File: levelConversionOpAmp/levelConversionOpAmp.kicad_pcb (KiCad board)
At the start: 2 copper layers, 38.1 x 61 mm, 23 parts, among them J1 IN, J2 OUT, J3 POW, Q1 PN2222A, Q2 PN2222A, U1 TL082

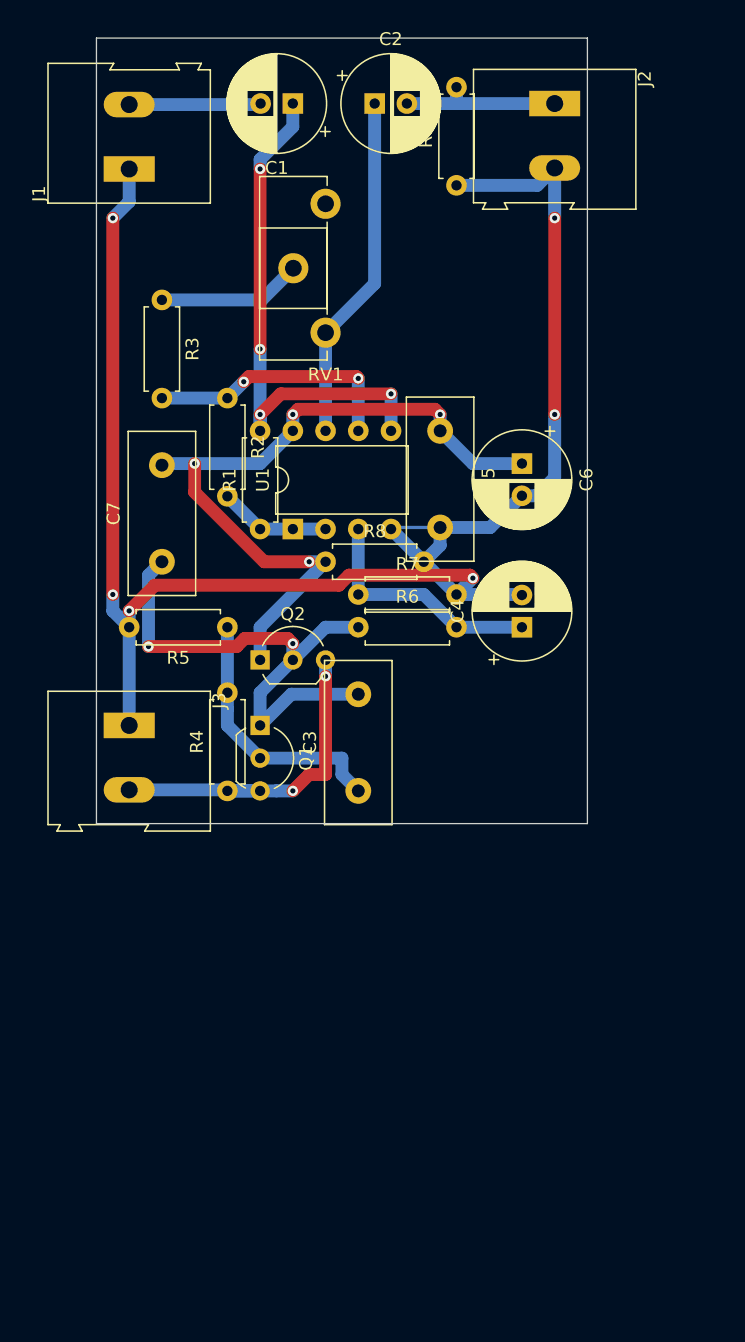
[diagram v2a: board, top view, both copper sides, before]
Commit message: Made PCB with surface mount and correct cap tolerances
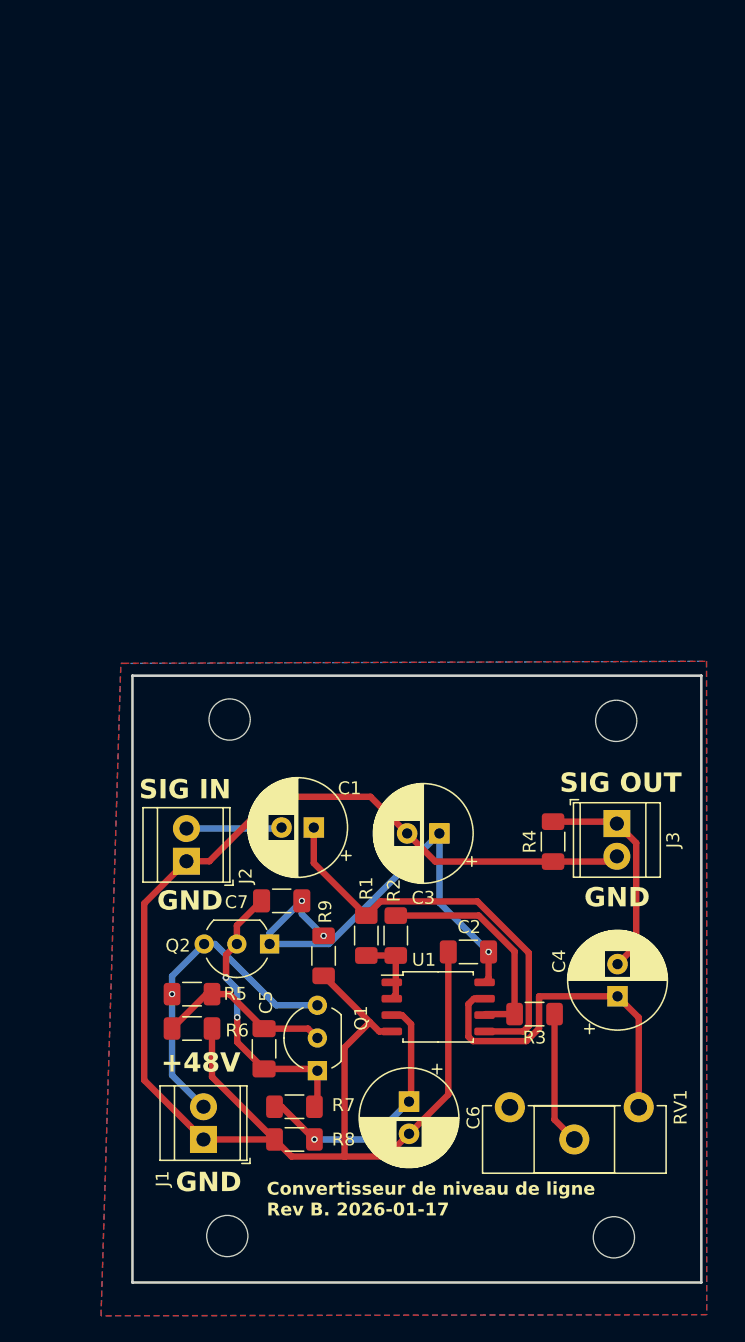
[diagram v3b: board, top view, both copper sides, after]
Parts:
- added REF1: MountingHole_3.2mm_M3_DIN965, MountingHole:MountingHole_3.2mm_M3_DIN965, F.Cu at (137.2, 141.2)
- added REF1: MountingHole_3.2mm_M3_DIN965, MountingHole:MountingHole_3.2mm_M3_DIN965, F.Cu at (167.2, 141.3)
- added REF1: MountingHole_3.2mm_M3_DIN965, MountingHole:MountingHole_3.2mm_M3_DIN965, F.Cu at (137.3, 101.1)
- added REF1: MountingHole_3.2mm_M3_DIN965, MountingHole:MountingHole_3.2mm_M3_DIN965, F.Cu at (167.3, 101.2)
- C1: value 10u/25V -> 47u/50V
- C2: value 100u/25V -> 1u; footprint Capacitor_THT:CP_Radial_D7.5mm_P2.50mm -> Capacitor_SMD:C_1206_3216Metric_Pad1.33x1.80mm_HandSolder
- C3: value 1u -> 47u/50V; footprint Capacitor_THT:C_Disc_D12.5mm_W5.0mm_P7.50mm -> Capacitor_THT:CP_Radial_D7.5mm_P2.50mm
- C4: value 47u/25V -> 47u/50V
- C5: value 100n -> 1u; footprint Capacitor_THT:C_Disc_D12.5mm_W5.0mm_P7.50mm -> Capacitor_SMD:C_1206_3216Metric_Pad1.33x1.80mm_HandSolder
- C6: value 220u/50V -> 47u/50V
- C7: footprint Capacitor_THT:C_Disc_D12.5mm_W5.0mm_P7.50mm -> Capacitor_SMD:C_1206_3216Metric_Pad1.33x1.80mm_HandSolder
- J1: value IN -> POW; footprint TerminalBlock:TerminalBlock_Altech_AK300-2_P5.00mm -> TerminalBlock_TE-Connectivity:TerminalBlock_TE_282834-2_1x02_P2.54mm_Horizontal
- J2: value OUT -> IN; footprint TerminalBlock:TerminalBlock_Altech_AK300-2_P5.00mm -> TerminalBlock_TE-Connectivity:TerminalBlock_TE_282834-2_1x02_P2.54mm_Horizontal
- J3: value POW -> OUT; footprint TerminalBlock:TerminalBlock_Altech_AK300-2_P5.00mm -> TerminalBlock_TE-Connectivity:TerminalBlock_TE_282834-2_1x02_P2.54mm_Horizontal
- R1, R2, R3, R5, R6, R7, R8: footprint Resistor_THT:R_Axial_DIN0207_L6.3mm_D2.5mm_P7.62mm_Horizontal -> Resistor_SMD:R_1206_3216Metric_Pad1.30x1.75mm_HandSolder
- R4: value 10k -> 4k7; footprint Resistor_THT:R_Axial_DIN0207_L6.3mm_D2.5mm_P7.62mm_Horizontal -> Resistor_SMD:R_1206_3216Metric_Pad1.30x1.75mm_HandSolder
- R9: value 4k7 -> 10k; footprint Resistor_THT:R_Axial_DIN0207_L6.3mm_D2.5mm_P7.62mm_Horizontal -> Resistor_SMD:R_1206_3216Metric_Pad1.30x1.75mm_HandSolder
- U1: footprint Package_DIP:DIP-8_W7.62mm -> Package_SO:SOIC-8_5.23x5.23mm_P1.27mm
- moved J1 75.5 mm to (135.3, 133.7)
- moved C2 66.2 mm to (155.9, 119.2), turned to 180 degrees
- moved J2 65.4 mm to (134.0, 112.1), turned to 90 degrees
- moved RV1 64.8 mm to (169.1, 131.2), turned to -90 degrees
- moved R3 62.5 mm to (161.0, 124.0), turned to 180 degrees
- moved R9 60.7 mm to (144.6, 119.5), turned to -90 degrees
- moved C1 56.2 mm to (143.9, 109.5)
- moved C6 50.3 mm to (151.3, 130.8)
- moved C5 49.9 mm to (140.0, 126.7), turned to 90 degrees
- moved R8 44.9 mm to (142.4, 133.7), turned to 180 degrees
- moved R2 43.7 mm to (150.2, 117.9)
- moved R7 40.1 mm to (142.4, 131.2), turned to 180 degrees
- moved U1 38.8 mm to (153.5, 123.4), turned to 0 degrees
- moved J3 38.6 mm to (167.4, 109.2)
- moved R6 33.7 mm to (134.4, 125.1)
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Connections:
- C2 pad 1: Net-(C2-Pad1) -> V+
- C2 pad 2: SIGOUT -> GND
- C3 pad 1: Net-(C3-Pad1) -> V+
- C3 pad 2: Net-(C3-Pad2) -> GND
- C4 pad 2: GND -> SIGOUT
- C5 pad 1: V+ -> Net-(Q1-E)
- C5 pad 2: GND -> Net-(Q1-B)
- C6 pad 1: V+ -> Net-(U1A-+)
- C7 pad 1: Net-(C3-Pad2) -> V+
- C7 pad 2: V+ -> Net-(Q1-E)
- J1 pad 2: SIGIN -> +48V
- J2 pad 1: SIGOUT -> GND
- J2 pad 2: GND -> SIGIN
- J3 pad 1: GND -> SIGOUT
- J3 pad 2: +48V -> GND
- Q1 pad 1: Net-(C3-Pad2) -> Net-(Q1-E)
- Q1 pad 2: Net-(C3-Pad1) -> Net-(Q1-B)
- Q2 pad 2: Net-(C3-Pad2) -> Net-(Q1-E)
- R4 pad 1: +48V -> GND
- R4 pad 2: Net-(C3-Pad1) -> SIGOUT
- R5 pad 1: Net-(C3-Pad1) -> +48V
- R5 pad 2: GND -> Net-(Q1-B)
- R6 pad 1: Net-(C3-Pad2) -> Net-(Q1-B)
- R6 pad 2: Net-(C4-Pad1) -> GND
- R7 pad 1: Net-(C4-Pad1) -> Net-(Q1-E)
- R7 pad 2: GND -> Net-(U1A-+)
- R8 pad 1: V+ -> Net-(U1A-+)
- R9 pad 1: GND -> V+
- R9 pad 2: SIGOUT -> GND
- RV1 pad 1: Net-(C2-Pad1) -> Net-(C4-Pad1)
- RV1 pad 3: (no net) -> unconnected-(RV1-Pad3)
- U1 pad 3: Net-(C4-Pad1) -> Net-(U1A-+)
- U1 pad 7: Net-(C2-Pad1) -> Net-(C4-Pad1)
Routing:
- net Net-(C3-Pad2): track 40.8 -> 0.00 mm, vias 2 -> 0
- net Net-(C2-Pad1): track 27.0 -> 0.00 mm
- net Net-(Q1-E): track 0.00 -> 22.5 mm, vias 0 -> 2
- net Net-(C3-Pad1): track 20.6 -> 0.00 mm
- net Net-(U1A-+): track 0.00 -> 20.6 mm, vias 0 -> 1
- net V+: track 57.3 -> 37.8 mm, vias 4 -> 3
- net Net-(Q1-B): track 0.00 -> 13.8 mm
- net GND: track 137.2 -> 124.1 mm, vias 6 -> 0
- net Net-(C4-Pad1): track 18.8 -> 27.8 mm
- net Net-(U1B-+): track 41.4 -> 32.5 mm, vias 4 -> 0
- net SIGOUT: track 12.7 -> 17.1 mm
- net VREF: track 8.67 -> 5.77 mm
- net SIGIN: track 10.2 -> 7.52 mm
- net Net-(U1B--): track 20.1 -> 17.6 mm, vias 2 -> 0
- net +48V: track 27.2 -> 25.4 mm, vias 2 -> 1
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- added copper zone on F.Cu, net GND
- added copper zone on B.Cu, net V+
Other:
- board size 38.1 x 61 mm -> 44.1 x 47.1 mm
- net class Default removed
- board text added: "+48V"
- board text added: "Convertisseur de niveau de ligne Rev B. 2026-01-17"
- board text added: "GND"
- board text added: "SIG IN"
- board text added: "SIG OUT"
